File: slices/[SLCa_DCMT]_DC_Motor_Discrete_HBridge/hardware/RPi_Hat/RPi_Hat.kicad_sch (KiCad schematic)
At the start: 1 part, among them J2 RPi_GPIO

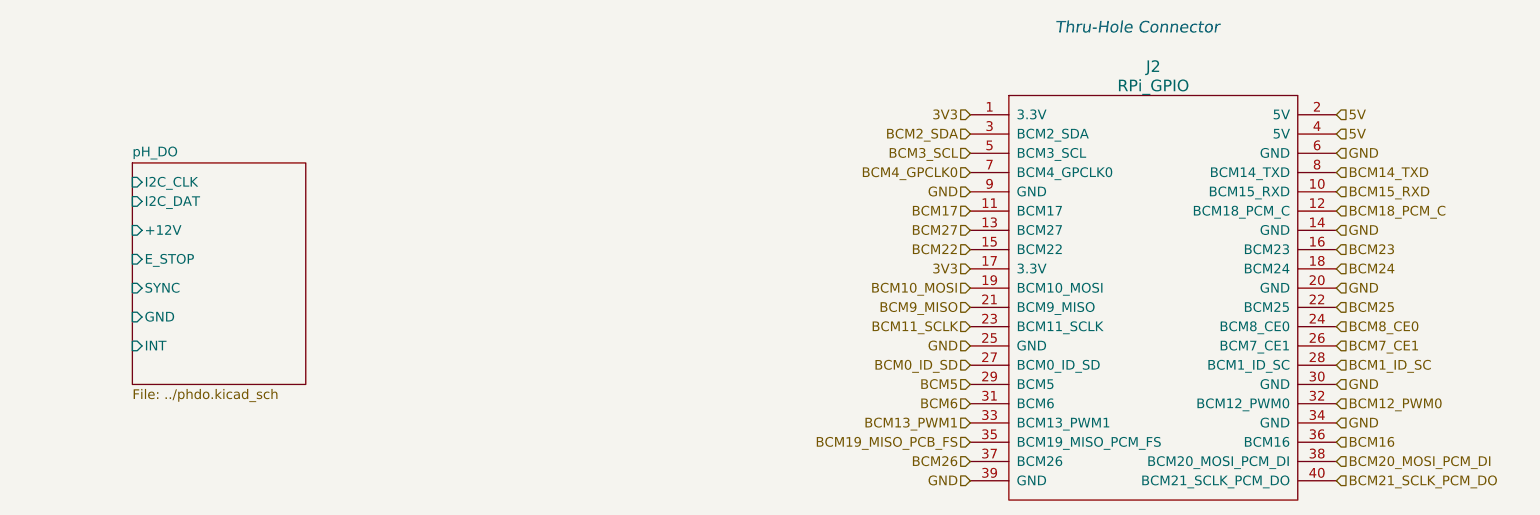
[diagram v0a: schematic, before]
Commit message: Initial commit of discrete hbridge motor driver
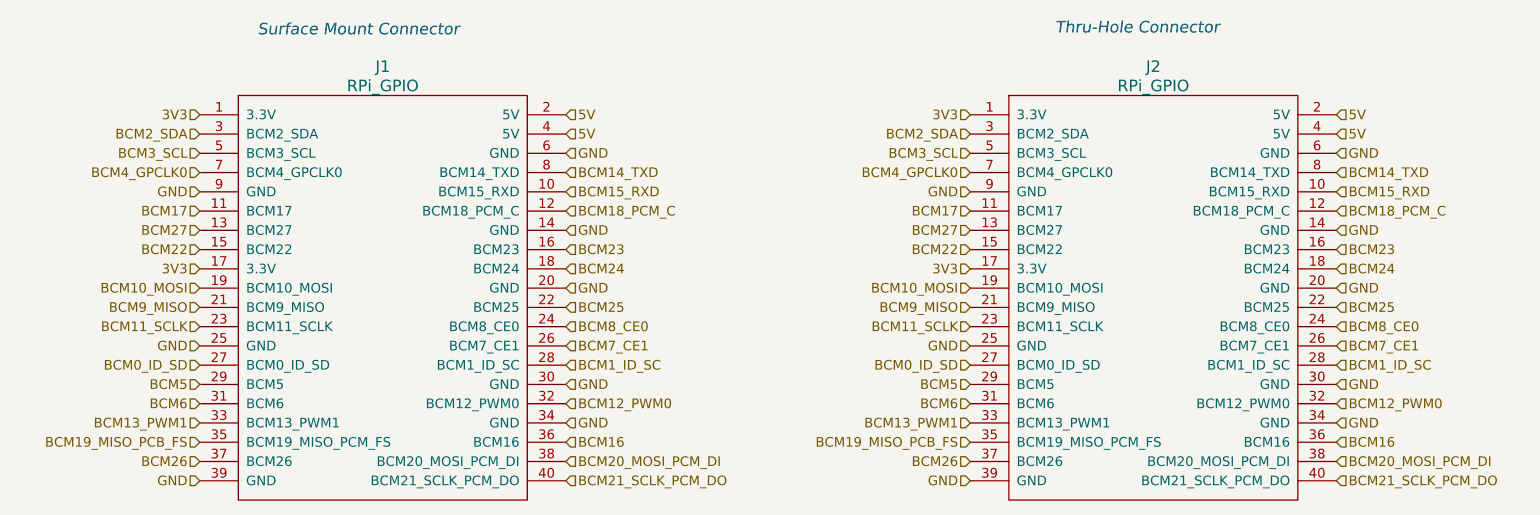
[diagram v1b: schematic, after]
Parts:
- added J1: RPi_GPIO, RPi_Hat:Samtec_HLE-120-02-XXX-DV-BE-XX-XX, symbol RPi_Hat1:RPi_GPIO_1
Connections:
- net 3V3: now also J1.1 (3.3V), J1.17 (3.3V)
- net 5V: now also J1.2 (5V), J1.4 (5V)
- net BCM0_ID_SD: now also J1.27 (BCM0_ID_SD)
- net BCM10_MOSI: now also J1.19 (BCM10_MOSI)
- net BCM11_SCLK: now also J1.23 (BCM11_SCLK)
- net BCM12_PWM0: now also J1.32 (BCM12_PWM0)
- net BCM13_PWM1: now also J1.33 (BCM13_PWM1)
- net BCM14_TXD: now also J1.8 (BCM14_TXD)
- net BCM15_RXD: now also J1.10 (BCM15_RXD)
- net BCM16: now also J1.36 (BCM16)
- net BCM17: now also J1.11 (BCM17)
- net BCM18_PCM_C: now also J1.12 (BCM18_PCM_C)
- net BCM19_MISO_PCB_FS: now also J1.35 (BCM19_MISO_PCM_FS)
- net BCM1_ID_SC: now also J1.28 (BCM1_ID_SC)
- net BCM20_MOSI_PCM_DI: now also J1.38 (BCM20_MOSI_PCM_DI)
- net BCM21_SCLK_PCM_DO: now also J1.40 (BCM21_SCLK_PCM_DO)
- net BCM22: now also J1.15 (BCM22)
- net BCM23: now also J1.16 (BCM23)
- net BCM24: now also J1.18 (BCM24)
- net BCM25: now also J1.22 (BCM25)
- net BCM26: now also J1.37 (BCM26)
- net BCM27: now also J1.13 (BCM27)
- net BCM2_SDA: now also J1.3 (BCM2_SDA)
- net BCM3_SCL: now also J1.5 (BCM3_SCL)
- net BCM4_GPCLK0: now also J1.7 (BCM4_GPCLK0)
- net BCM5: now also J1.29 (BCM5)
- net BCM6: now also J1.31 (BCM6)
- net BCM7_CE1: now also J1.26 (BCM7_CE1)
- net BCM8_CE0: now also J1.24 (BCM8_CE0)
- net BCM9_MISO: now also J1.21 (BCM9_MISO)
- net GND: now also J1.14 (GND), J1.20 (GND), J1.25 (GND), J1.30 (GND), J1.34 (GND), J1.39 (GND), J1.6 (GND), J1.9 (GND)
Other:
- removed sheet pH_DO
- note added: "Surface Mount Connector"
